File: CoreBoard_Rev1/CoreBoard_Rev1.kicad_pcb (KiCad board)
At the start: 2 copper layers, 90 parts, among them J1 RJ45_LED_Shielded, SW1 SW_Push, SW10 SW_Push, SW11 SW_Push, SW12 SW_Push, SW13 SW_Push, SW14 SW_Push, SW15 SW_Push, SW16 SW_SPDT, SW2 SW_Push, SW3 SW_Push, SW4 SW_Push, SW5 SW_Push, SW6 SW_Push, SW7 SW_Push, SW8 SW_Push, SW9 SW_Push, U1 Teensy4.1_DEV-16771, U2 TSR_1-2450, U4 74HC148, U5 74HC148, U6 74HC00, U7 OKI

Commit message: re-did board
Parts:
- Conn2, Conn3, Conn4, Conn5, Conn6: footprint MRDT_Connectors:MOLEX_SL_09_Vertical -> MRDT_Connectors:MOLEX_SL_09_Horizontal
- moved REF** 342.3 mm to (85.9, 63.8), turned to 180 degrees
- moved R33 305.0 mm to (109.1, 85.4), turned to 0 degrees
- moved R28 304.3 mm to (105.3, 85.4)
- moved D18 298.0 mm to (113.1, 85.4), turned to 0 degrees
- moved R32 295.4 mm to (121.7, 64.5), turned to 0 degrees
- moved R27 294.9 mm to (118.0, 64.5)
- moved SW15 291.1 mm to (110.0, 89.6), turned to 180 degrees
- moved D17 288.8 mm to (125.6, 64.5), turned to 0 degrees
- moved SW14 283.5 mm to (121.1, 68.6), turned to 180 degrees
- moved R23 257.1 mm to (121.8, 85.3), turned to 0 degrees
- moved R18 256.7 mm to (118.0, 85.3)
- moved R31 252.0 mm to (155.9, 73.2), turned to 0 degrees
- moved REF** 251.9 mm to (85.9, 140.0), turned to 180 degrees
- moved R26 251.1 mm to (152.3, 73.2)
- moved D13 249.8 mm to (125.8, 85.3), turned to 0 degrees
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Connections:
- U1 pad 0: FL_RX -> unconnected-(U1-RX1-Pad0)
- U1 pad 1: FL_TX -> unconnected-(U1-TX1-Pad1)
- U1 pad 10: unconnected-(U1-CS1-Pad10) -> ServoPWM9
- U1 pad 12: ServoPWM7 -> unconnected-(U1-MISO-Pad12)
- U1 pad 14: BR_RX -> FL_RX
- U1 pad 15: BR_TX -> unconnected-(U1-A1-Pad15)
- U1 pad 16: FR_RX -> BR_TX
- U1 pad 17: FR_TX -> BR_RX
- U1 pad 18: ServoPWM9 -> Out1
- U1 pad 19: ServoPWM8 -> Out0
- U1 pad 2: ServoPWM4 -> ServoPWM1
- U1 pad 22: unconnected-(U1-A8-Pad22) -> FR_TX
- U1 pad 23: unconnected-(U1-A9-Pad23) -> FR_RX
- U1 pad 24: Out3 -> unconnected-(U1-A10-Pad24)
- U1 pad 25: Out2 -> unconnected-(U1-A11-Pad25)
- U1 pad 28: BL_TX -> unconnected-(U1-RX7-Pad28)
- U1 pad 29: BL_RX -> unconnected-(U1-TX7-Pad29)
- U1 pad 3: ServoPWM1 -> ServoPWM2
- U1 pad 30: unconnected-(U1-CRX3-Pad30) -> BL_TX
- U1 pad 33: ServoPWM3 -> Out3
- U1 pad 34: unconnected-(U1-RX8-Pad34) -> Out2
- U1 pad 35: unconnected-(U1-TX8-Pad35) -> BL_RX
- U1 pad 36: Out1 -> ML_TX
- U1 pad 37: Out0 -> ML_RX
- U1 pad 38: unconnected-(U1-A14-Pad38) -> FL_TX
- U1 pad 4: ServoPWM2 -> ServoPWM3
- U1 pad 5: unconnected-(U1-IN2-Pad5) -> ServoPWM4
- U1 pad 7: ML_RX -> ServoPWM6
- U1 pad 8: ML_TX -> ServoPWM7
- U1 pad 9: ServoPWM6 -> ServoPWM8
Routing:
- net +3V3: track 602.5 -> 245.6 mm
- net Out1: track 101.4 -> 0.00 mm, vias 8 -> 0
- net B5: track 97.9 -> 0.00 mm, vias 2 -> 0
- net +5V: track 132.0 -> 226.4 mm, vias 3 -> 1
- net Out0: track 94.2 -> 0.00 mm, vias 5 -> 0
- net B9: track 85.2 -> 0.00 mm, vias 2 -> 0
- net B10: track 81.0 -> 0.00 mm, vias 2 -> 0
- net Out2: track 79.8 -> 0.00 mm, vias 7 -> 0
- net B6: track 77.3 -> 0.00 mm, vias 2 -> 0
- net B4: track 73.4 -> 0.00 mm, vias 2 -> 0
- net B8: track 70.1 -> 0.00 mm, vias 2 -> 0
- net B7: track 65.5 -> 0.00 mm, vias 2 -> 0
- net B12: track 92.7 -> 27.3 mm, vias 4 -> 0
- net PV: track 84.3 -> 23.5 mm, vias 1 -> 0
- net B3: track 59.7 -> 0.00 mm, vias 4 -> 0
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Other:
- board outline added: 128.8 x 84.3 mm
- board text added: "12V"
- board text added: "3V"
- board text added: "5V"
- board text added: "BL"
- board text added: "BR"
- board text added: "FL"
- board text added: "FR"
- board text added: "Label 1"
- board text added: "Label 2"
- board text added: "Label 3"
- board text added: "Left Motors"
- board text added: "ML"
- board text added: "MR"
- board text added: "Reverse"
- board text added: "Right Motors"
- board text added: "S1"
- board text added: "S2"
- board text added: "S3"
- board text added: "S4"
- board text added: "S5"
- board text added: "S6"
- board text added: "S7"
- board text added: "S8"
- board text added: "S9"

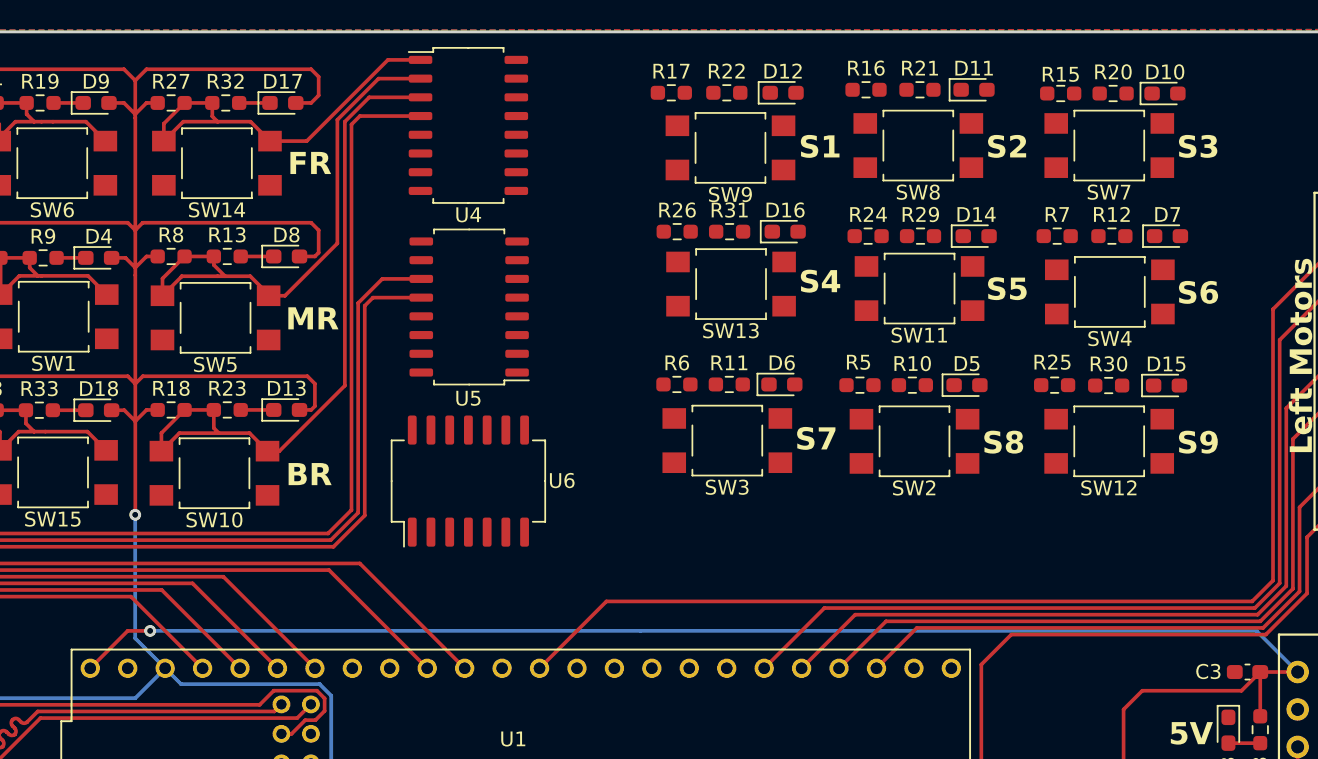
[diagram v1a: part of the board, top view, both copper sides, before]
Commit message: More Buttons
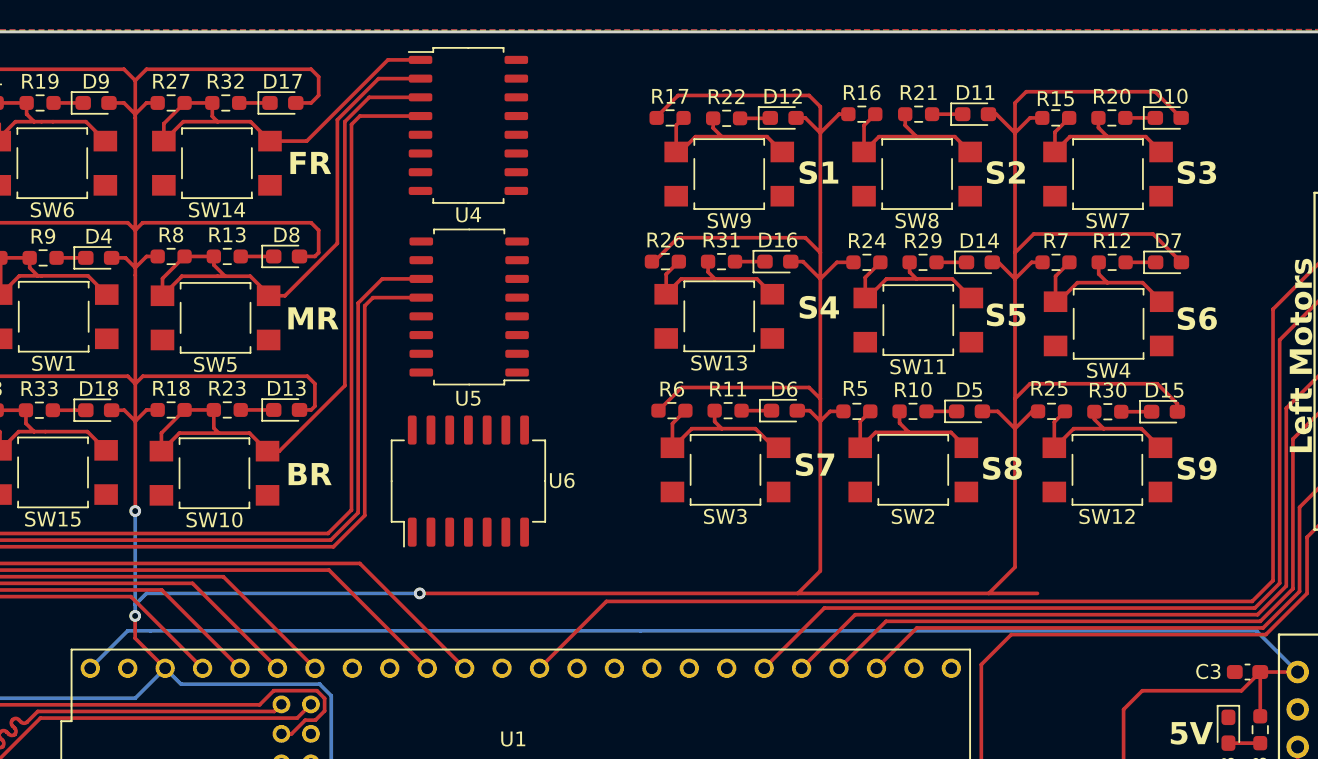
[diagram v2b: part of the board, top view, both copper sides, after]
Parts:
- moved SW13 2.33 mm to (155.2, 79.0)
- moved R26 2.18 mm to (151.5, 75.3)
- moved SW4 2.17 mm to (181.6, 79.5)
- moved SW11 2.14 mm to (168.7, 79.2)
- moved R31 2.10 mm to (155.3, 75.3)
- moved D16 2.09 mm to (159.2, 75.3)
- moved SW3 1.99 mm to (155.6, 89.4)
- moved SW12 1.94 mm to (181.5, 89.4)
- moved SW2 1.94 mm to (168.4, 89.4)
- moved SW7 1.94 mm to (181.6, 69.3)
- moved SW8 1.94 mm to (168.6, 69.3)
- moved R6 1.81 mm to (152.0, 85.4)
- moved D14 1.79 mm to (172.8, 75.3)
- moved R5 1.79 mm to (164.5, 85.4)
- moved R25 1.79 mm to (177.7, 85.4)
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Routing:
- net +3V3: track 245.6 -> 475.9 mm, vias 1 -> 3
- net B8: track 0.00 -> 12.8 mm
- net B10: track 0.00 -> 12.8 mm
- net B7: track 0.00 -> 12.6 mm
- net B4: track 0.00 -> 12.5 mm
- net B6: track 0.00 -> 12.4 mm
- net B5: track 0.00 -> 12.3 mm
- net B3: track 0.00 -> 12.3 mm
- net B9: track 0.00 -> 12.0 mm
- net B11: track 0.00 -> 11.8 mm
- net Net-(D11-K): track 0.00 -> 2.08 mm
- net Net-(D12-K): track 0.00 -> 2.06 mm
- net Net-(D15-K): track 0.00 -> 2.06 mm
- net Net-(D5-K): track 0.00 -> 2.05 mm
- net Net-(D10-K): track 0.00 -> 2.04 mm
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
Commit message: More Encoder Work
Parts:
- moved U6 1.52 mm to (138.2, 91.7)
- moved U5 0.91 mm to (138.4, 79.2)
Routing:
- net B5: track 12.3 -> 96.2 mm, vias 0 -> 2
- net B6: track 12.4 -> 63.7 mm, vias 0 -> 2
- net B4: track 12.5 -> 48.6 mm
- net +3V3: track 475.9 -> 506.5 mm, vias 3 -> 9
- net B9: track 12.0 -> 31.2 mm
- net B7: track 12.6 -> 31.0 mm
- net B11: track 11.8 -> 25.7 mm
- net B8: track 12.8 -> 14.8 mm
- net B10: track 12.8 -> 14.8 mm
- net B3: track 12.3 -> 14.3 mm
- net B1: track 83.0 -> 82.2 mm
- net B2: track 94.5 -> 93.7 mm

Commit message: More Encoder Work
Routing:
- net B10: track 14.8 -> 63.3 mm, vias 0 -> 2
- net Out2: track 0.00 -> 37.5 mm, vias 0 -> 1
- net B8: track 14.8 -> 50.2 mm, vias 0 -> 2
- net B3: track 14.3 -> 45.0 mm, vias 0 -> 2
- net +3V3: track 506.5 -> 525.5 mm, vias 9 -> 10
- net Out0: track 0.00 -> 11.9 mm, vias 0 -> 1
- net Out1: track 0.00 -> 11.9 mm, vias 0 -> 1
- net +5V: track 226.4 -> 229.1 mm
- net FR_RX: track 32.6 -> 33.6 mm

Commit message: connected remaining components
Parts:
- U2: footprint Converter_DCDC:Converter_DCDC_TRACO_TSR-1_THT -> MRDT_Devices:SHHD003A0A-SRZ
- moved U2 70.1 mm to (176.6, 68.4), turned to -90 degrees
- moved R38 51.3 mm to (142.0, 95.2), turned to 90 degrees
- moved R12 49.5 mm to (140.6, 47.9)
- moved R7 49.5 mm to (136.8, 47.9)
- moved D7 49.5 mm to (144.5, 47.9)
- moved SW4 48.8 mm to (141.5, 51.7)
- moved D23 47.2 mm to (144.0, 95.2), turned to 90 degrees
- moved R35 46.5 mm to (153.2, 95.2), turned to 90 degrees
- moved D20 43.6 mm to (155.2, 95.2), turned to 90 degrees
- moved R30 38.2 mm to (154.6, 58.4)
- moved R25 38.2 mm to (150.7, 58.4)
- moved D15 38.2 mm to (158.4, 58.4)
- moved SW2 37.7 mm to (169.4, 51.7)
- moved SW3 37.7 mm to (155.4, 51.7)
- moved SW12 37.7 mm to (155.4, 62.2)
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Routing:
- net +3V3: track 525.5 -> 641.1 mm, vias 10 -> 8
- net Out3: track 0.00 -> 76.7 mm, vias 0 -> 4
- net PV: track 23.5 -> 75.7 mm, vias 0 -> 1
- net Net-(U2-Vout): track 0.00 -> 43.4 mm
- net +5V: track 229.1 -> 269.5 mm, vias 0 -> 1
- net B3: track 45.0 -> 83.0 mm
- net B8: track 50.2 -> 84.7 mm, vias 2 -> 0
- net B7: track 31.0 -> 64.2 mm
- net Net-(U4-S2): track 0.00 -> 33.0 mm, vias 0 -> 4
- net B10: track 63.3 -> 31.8 mm, vias 2 -> 0
- net Net-(U4-S1): track 0.00 -> 29.7 mm, vias 0 -> 4
- net B4: track 48.5 -> 77.9 mm
- net Net-(U4-S0): track 0.00 -> 29.2 mm, vias 0 -> 2
- net Net-(U5-S2): track 0.18 -> 26.9 mm, vias 0 -> 4
- net Net-(U5-S1): track 0.00 -> 25.1 mm, vias 0 -> 4
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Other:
- board size 128.8 x 84.3 mm -> 135.1 x 84.3 mm
- board text added: "Servo 1-3"
- board text added: "Servo 4-6"
- board text added: "Servo 7-9"
- board text added: "logo here?"
- board text added: "lots of islands, make grounding better"
- board text added: "make everything more aligned generally nicer looking"
- board text added: "redo left buttons please <3"
- board text removed: "Label 1"
- board text removed: "Label 2"
- board text removed: "Label 3"

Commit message: more aligning
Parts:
- moved Conn6 3.09 mm to (158.2, 103.1)
- moved Conn5 2.09 mm to (130.6, 103.1)
- moved Conn1 1.27 mm to (168.0, 98.2)
- moved Conn4 0.92 mm to (102.9, 103.1)
- moved R18 0.53 mm to (104.4, 58.4)
- moved R23 0.53 mm to (108.3, 58.4)
- moved D13 0.51 mm to (112.1, 58.4)
- moved D18 0.50 mm to (99.3, 58.4)
- moved R33 0.49 mm to (95.4, 58.4)
- moved R28 0.49 mm to (91.5, 58.4)
- moved R13 0.41 mm to (108.3, 47.9)
- moved R8 0.41 mm to (104.4, 47.9)
- moved R4 0.38 mm to (91.5, 47.9)
- moved D8 0.38 mm to (112.1, 47.9)
- moved R9 0.37 mm to (95.4, 47.9)
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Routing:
- net +3V3: track 641.1 -> 647.9 mm
- net B15: track 78.7 -> 82.6 mm
- net +5V: track 269.5 -> 273.2 mm
- net ServoPWM8: track 31.7 -> 28.9 mm
- net ServoPWM9: track 37.9 -> 35.1 mm
- net ServoPWM7: track 25.5 -> 22.7 mm
- net B5: track 88.5 -> 90.5 mm
- net B4: track 77.9 -> 79.9 mm
- net B3: track 83.0 -> 85.0 mm
- net B9: track 39.8 -> 41.8 mm
- net B8: track 84.7 -> 86.7 mm
- net B7: track 64.2 -> 66.2 mm
- net B11: track 22.6 -> 24.6 mm
- net B14: track 47.8 -> 45.9 mm
- net ServoPWM6: track 22.3 -> 20.5 mm
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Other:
- board text removed: "make everything more aligned generally nicer looking"
- board text removed: "redo left buttons please <3"

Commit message: all but logo (allegedly)
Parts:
- moved C2 0.76 mm to (180.6, 99.2)
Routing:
- net +3V3: track 647.9 -> 650.7 mm, vias 8 -> 9
- net PV: track 75.6 -> 76.8 mm
- net GND: vias 0 -> 19
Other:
- board text removed: "lots of islands, make grounding better"

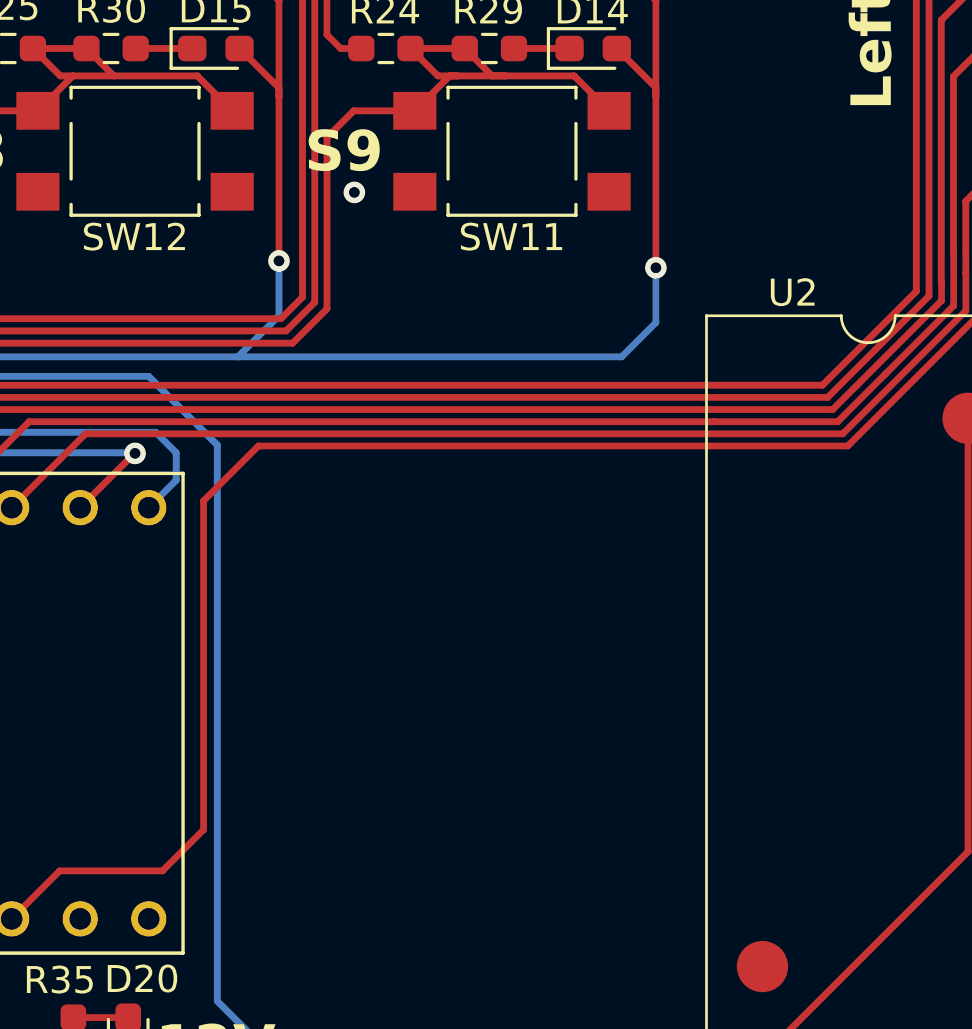
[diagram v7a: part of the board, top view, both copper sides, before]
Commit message: Logo and Names Added to Layout
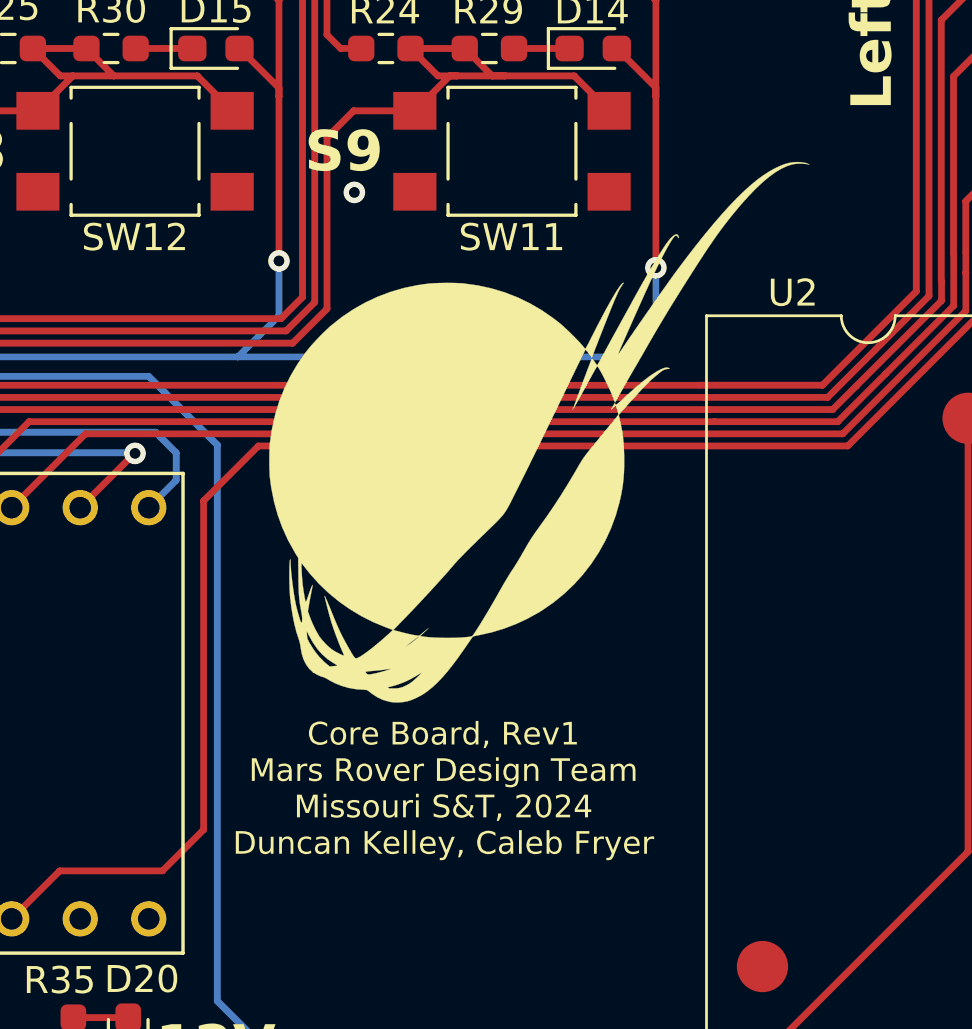
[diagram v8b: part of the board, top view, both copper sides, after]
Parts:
- added G***: LOGO, MRDT_Silkscreens:0_MRDT_Logo_20mm, F.Cu at (170.4, 72.6)
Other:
- board text added: "Core Board, Rev1 Mars Rover Design Team Missouri S&T, 2024 Duncan Kelley, Caleb Fryer"
- board text removed: "logo here?"
